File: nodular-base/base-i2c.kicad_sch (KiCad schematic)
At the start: 4 parts, among them U4 TCA9548APWR, U7 SC7A20

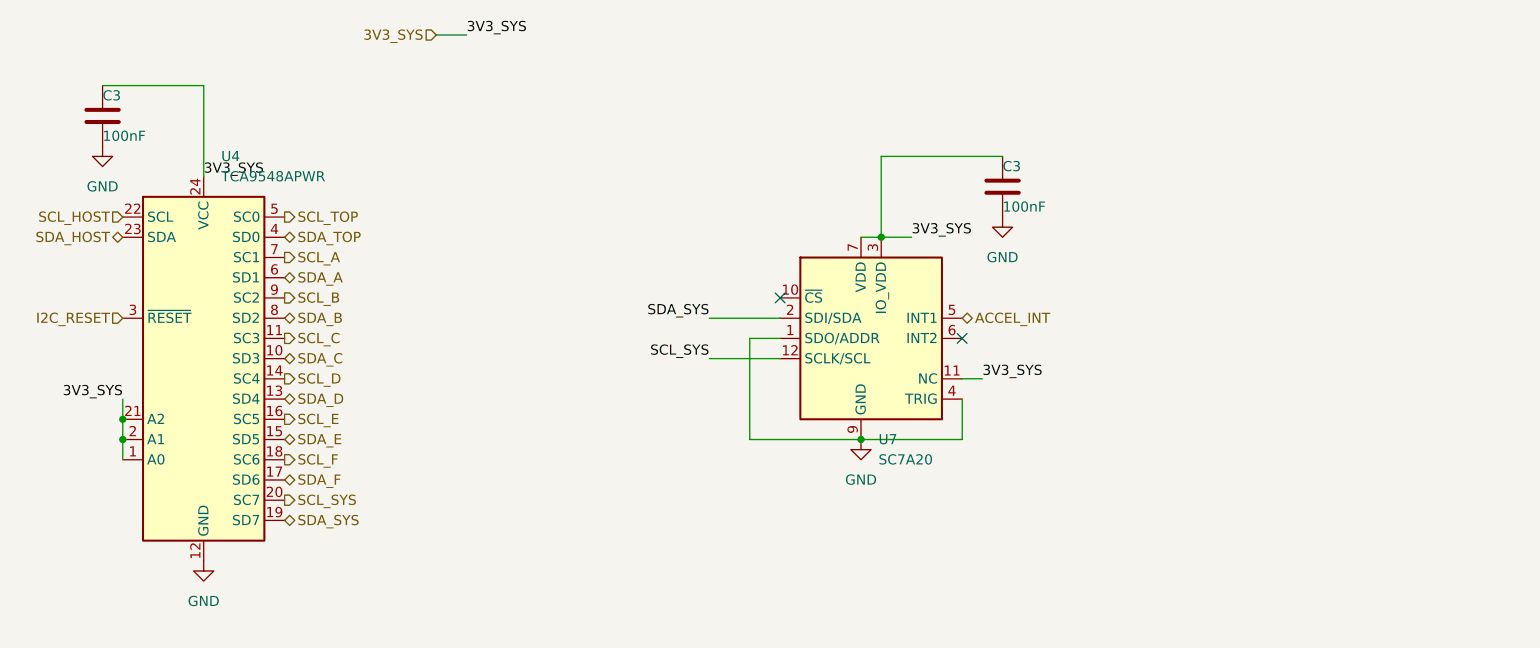
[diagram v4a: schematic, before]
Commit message: Add additional accelerometer-gyro option, update pin and address map, fix some ERC errors
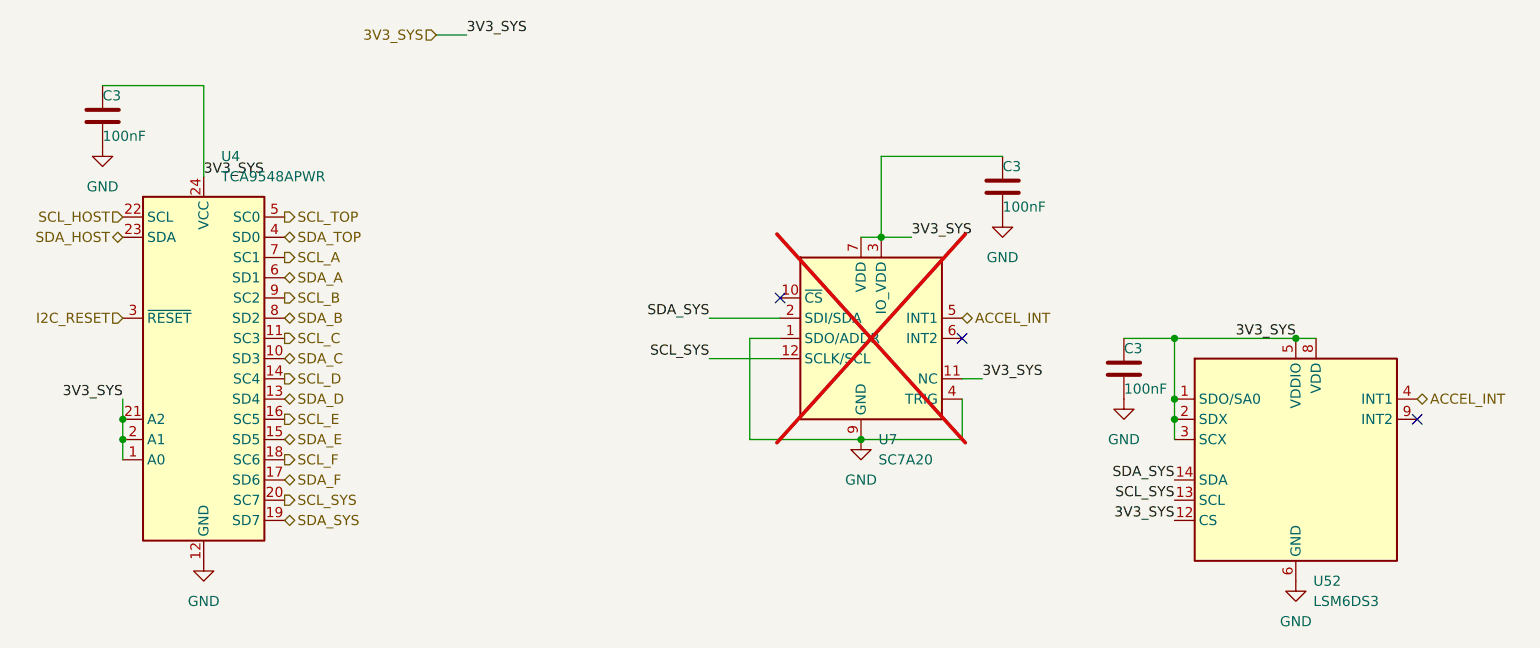
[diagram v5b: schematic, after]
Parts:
- added C3: 100nF, Capacitor_SMD:C_0402_1005Metric, symbol Device:C
- added U52: LSM6DS3, Package_LGA:LGA-14_3x2.5mm_P0.5mm_LayoutBorder3x4y, symbol Sensor_Motion:LSM6DS3
- U7: now not fitted
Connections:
- net 3V3_SYS: now also C3.1, U52.1 (SDO/SA0), U52.12 (CS), U52.2 (SDX), U52.3 (SCX), U52.5 (VDDIO), U52.8 (VDD)
- net ACCEL_INT: now also U52.4 (INT1)
- net GND: now also C3.2, U52.6 (GND), U52.7 (GND)
- net SCL_SYS: now also U52.13 (SCL)
- net SDA_SYS: now also U52.14 (SDA)
- no-connect marks 2 -> 3
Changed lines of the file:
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@@
 (kicad_sch (version 20230121) (generator eeschema)
   (paper "A4")
+  (junction (at 234.95 80.01) (diameter 0) (color 0 0 0 0)
+  )
+  (junction (at 234.95 82.55) (diameter 0) (color 0 0 0 0)
+  )
   (junction (at 102.87 85.09) (diameter 0) (color 0 0 0 0)
   )
+  (junction (at 250.19 72.39) (diameter 0) (color 0 0 0 0)
+  )
   (junction (at 102.87 82.55) (diameter 0) (color 0 0 0 0)
+  )
+  (junction (at 234.95 72.39) (diameter 0) (color 0 0 0 0)
   )
   (junction (at 198.12 59.69) (diameter 0) (color 0 0 0 0)
@@
   (no_connect (at 208.28 72.39))
   (no_connect (at 185.42 67.31))
+  (no_connect (at 265.43 82.55))
   (wire (pts (xy 102.87 82.55) (xy 102.87 85.09))
     (stroke (width 0) (type default))
@@
     (stroke (width 0) (type default))
   )
+  (wire (pts (xy 234.95 80.01) (xy 234.95 72.39))
+    (stroke (width 0) (type default))
+  )
   (wire (pts (xy 213.36 49.53) (xy 198.12 49.53))
     (stroke (width 0) (type default))
   )
+  (wire (pts (xy 228.6 72.39) (xy 234.95 72.39))
+    (stroke (width 0) (type default))
+  )
   (wire (pts (xy 102.87 80.01) (xy 102.87 82.55))
     (stroke (width 0) (type default))
@@
     (stroke (width 0) (type default))
   )
+  (wire (pts (xy 234.95 82.55) (xy 234.95 80.01))
+    (stroke (width 0) (type default))
+  )
   (wire (pts (xy 113.03 52.07) (xy 113.03 40.64))
     (stroke (width 0) (type default))
   )
+  (wire (pts (xy 234.95 85.09) (xy 234.95 82.55))
+    (stroke (width 0) (type default))
+  )
   (wire (pts (xy 195.58 59.69) (xy 198.12 59.69))
     (stroke (width 0) (type default))
   )
+  (wire (pts (xy 234.95 72.39) (xy 250.19 72.39))
+    (stroke (width 0) (type default))
+  )
   (wire (pts (xy 198.12 49.53) (xy 198.12 59.69))
     (stroke (width 0) (type default))
@@
   )
   (wire (pts (xy 208.28 80.01) (xy 208.28 85.09))
+    (stroke (width 0) (type default))
+  )
+  (wire (pts (xy 250.19 72.39) (xy 252.73 72.39))
     (stroke (width 0) (type default))
   )
@@
     (effects (font (size 1.27 1.27)) (justify left bottom))
   )
+  (label "3V3_SYS" (at 234.95 95.25 180) (fields_autoplaced)
+    (effects (font (size 1.27 1.27)) (justify right bottom))
+  )
+  (label "SCL_SYS" (at 234.95 92.71 180) (fields_autoplaced)
+    (effects (font (size 1.27 1.27)) (justify right bottom))
+  )
   (label "SCL_SYS" (at 176.53 74.93 180) (fields_autoplaced)
+    (effects (font (size 1.27 1.27)) (justify right bottom))
+  )
+  (label "3V3_SYS" (at 250.19 72.39 180) (fields_autoplaced)
+    (effects (font (size 1.27 1.27)) (justify right bottom))
+  )
+  (label "SDA_SYS" (at 234.95 90.17 180) (fields_autoplaced)
     (effects (font (size 1.27 1.27)) (justify right bottom))
   )
@@
     (effects (font (size 1.27 1.27)) (justify left))
   )
+  (hierarchical_label "ACCEL_INT" (shape bidirectional) (at 265.43 80.01 0) (fields_autoplaced)
+    (effects (font (size 1.27 1.27)) (justify left))
+  )
   (hierarchical_label "SCL_A" (shape output) (at 123.19 62.23 0) (fields_autoplaced)
     (effects (font (size 1.27 1.27)) (justify left))
+  )
+  (symbol (lib_id "power:GND") (at 250.19 102.87 0) (unit 1)
+    (in_bom yes) (on_board yes) (dnp no) (fields_autoplaced)
+    (property "Reference" "#PWR070" (at 250.19 109.22 0)
+      (effects (font (size 1.27 1.27)) hide)
+    )
+    (property "Value" "GND" (at 250.19 107.95 0)
+      (effects (font (size 1.27 1.27)))
+    )
+    (property "Footprint" "" (at 250.19 102.87 0)
+      (effects (font (size 1.27 1.27)) hide)
+    )
+    (property "Datasheet" "" (at 250.19 102.87 0)
+      (effects (font (size 1.27 1.27)) hide)
+    )
+    (pin "1")
+    (instances
+      (project "nodular-base"
+        (path "/6dcb0502-87e2-4c28-9ce8-81aab8925f06/5ae693f9-48f3-406c-bbdf-b76d81cc71eb"
+          (reference "#PWR070") (unit 1)
+        )
+      )
+    )
   )
   (symbol (lib_id "Interface_Expansion:TCA9548APWR") (at 113.03 74.93 0) (unit 1)
@@
     )
   )
+  (symbol (lib_id "power:GND") (at 228.6 80.01 0) (unit 1)
+    (in_bom yes) (on_board yes) (dnp no) (fields_autoplaced)
+    (property "Reference" "#PWR071" (at 228.6 86.36 0)
+      (effects (font (size 1.27 1.27)) hide)
+    )
+    (property "Value" "GND" (at 228.6 85.09 0)
+      (effects (font (size 1.27 1.27)))
+    )
+    (property "Footprint" "" (at 228.6 80.01 0)
+      (effects (font (size 1.27 1.27)) hide)
+    )
+    (property "Datasheet" "" (at 228.6 80.01 0)
+      (effects (font (size 1.27 1.27)) hide)
+    )
+    (pin "1")
+    (instances
+      (project "nodular-base"
+        (path "/6dcb0502-87e2-4c28-9ce8-81aab8925f06/5ae693f9-48f3-406c-bbdf-b76d81cc71eb"
+          (reference "#PWR071") (unit 1)
+        )
+      )
+    )
+  )
   (symbol (lib_id "Device:C") (at 100.33 44.45 0) (unit 1)
     (in_bom yes) (on_board yes) (dnp no)
@@
     )
   )
+  (symbol (lib_id "Device:C") (at 228.6 76.2 0) (unit 1)
+    (in_bom yes) (on_board yes) (dnp no)
+    (property "Reference" "C3" (at 228.6 73.66 0)
+      (effects (font (size 1.27 1.27)) (justify left))
+    )
+    (property "Value" "100nF" (at 228.6 78.74 0)
+      (effects (font (size 1.27 1.27)) (justify left))
+    )
+    (property "Footprint" "Capacitor_SMD:C_0402_1005Metric" (at 229.5652 80.01 0)
+      (effects (font (size 1.27 1.27)) hide)
+    )
+    (property "Datasheet" "~" (at 228.6 76.2 0)
+      (effects (font (size 1.27 1.27)) hide)
+    )
+    (pin "1")
+    (pin "2")
+    (instances
+      (project "nodular-base"
+        (path "/6dcb0502-87e2-4c28-9ce8-81aab8925f06"
+          (reference "C3") (unit 1)
+        )
+        (path "/6dcb0502-87e2-4c28-9ce8-81aab8925f06/5ae693f9-48f3-406c-bbdf-b76d81cc71eb"
+          (reference "C50") (unit 1)
+        )
+      )
+    )
+  )
   (symbol (lib_id "power:GND") (at 213.36 57.15 0) (unit 1)
     (in_bom yes) (on_board yes) (dnp no) (fields_autoplaced)
@@
     )
   )
+  (symbol (lib_id "Sensor_Motion:LSM6DS3") (at 250.19 87.63 0) (unit 1)
+    (in_bom yes) (on_board yes) (dnp no) (fields_autoplaced)
+    (property "Reference" "U52" (at 252.3841 102.87 0)
+      (effects (font (size 1.27 1.27)) (justify left))
+    )
+    (property "Value" "LSM6DS3" (at 252.3841 105.41 0)
+      (effects (font (size 1.27 1.27)) (justify left))
+    )
+    (property "Footprint" "Package_LGA:LGA-14_3x2.5mm_P0.5mm_LayoutBorder3x4y" (at 240.03 105.41 0)
+      (effects (font (size 1.27 1.27)) (justify left) hide)
+    )
+    (property "Datasheet" "https://www.st.com/resource/en/datasheet/lsm6ds3tr-c.pdf" (at 252.73 104.14 0)
+      (effects (font (size 1.27 1.27)) hide)
+    )
+    (pin "13")
+    (pin "11")
+    (pin "2")
+    (pin "12")
+    (pin "7")
+    (pin "14")
+    (pin "5")
+    (pin "6")
+    (pin "8")
+    (pin "4")
+    (pin "3")
+    (pin "10")
+    (pin "9")
+    (pin "1")
+    (instances
+      (project "nodular-base"
+        (path "/6dcb0502-87e2-4c28-9ce8-81aab8925f06/5ae693f9-48f3-406c-bbdf-b76d81cc71eb"
+          (reference "U52") (unit 1)
+        )
+      )
+    )
+  )
   (symbol (lib_id "power:GND") (at 100.33 48.26 0) (unit 1)
     (in_bom yes) (on_board yes) (dnp no) (fields_autoplaced)
@@
   )
   (symbol (lib_id "Sensor_Motion:KX022-1020") (at 195.58 72.39 0) (unit 1)
-    (in_bom yes) (on_board yes) (dnp no) (fields_autoplaced)
+    (in_bom yes) (on_board yes) (dnp yes) (fields_autoplaced)
     (property "Reference" "U7" (at 197.7741 85.09 0)
       (effects (font (size 1.27 1.27)) (justify left))

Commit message: Modify base board: - Fix ESP32 strapping pins state - Remove 3/6 M3 standoffs - Change to LGA-style pads on ESP32 - Modify SFP mechanical pads to not be plated - Add larger mechanical pads with more solder paste surface to USB-C connectors
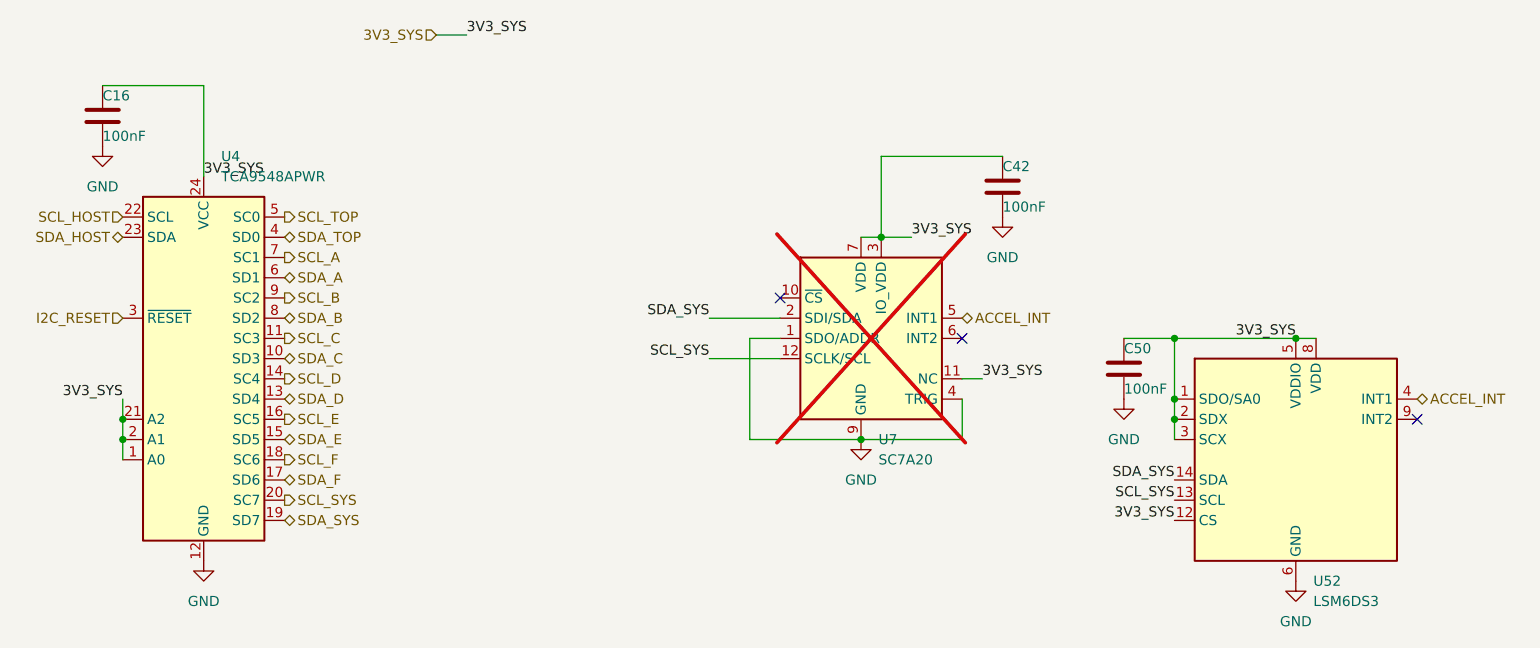
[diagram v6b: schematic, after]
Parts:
- renumbered C3 to C16, C3 to C42, C3 to C50
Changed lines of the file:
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@@
   (symbol (lib_id "Device:C") (at 213.36 53.34 0) (unit 1)
     (in_bom yes) (on_board yes) (dnp no)
-    (property "Reference" "C3" (at 213.36 50.8 0)
+    (property "Reference" "C42" (at 213.36 50.8 0)
       (effects (font (size 1.27 1.27)) (justify left))
     )
@@
     (instances
       (project "nodular-base"
-        (path "/6dcb0502-87e2-4c28-9ce8-81aab8925f06"
-          (reference "C3") (unit 1)
-        )
         (path "/6dcb0502-87e2-4c28-9ce8-81aab8925f06/5ae693f9-48f3-406c-bbdf-b76d81cc71eb"
           (reference "C42") (unit 1)
@@
   (symbol (lib_id "Device:C") (at 100.33 44.45 0) (unit 1)
     (in_bom yes) (on_board yes) (dnp no)
-    (property "Reference" "C3" (at 100.33 41.91 0)
+    (property "Reference" "C16" (at 100.33 41.91 0)
       (effects (font (size 1.27 1.27)) (justify left))
     )
@@
     (instances
       (project "nodular-base"
-        (path "/6dcb0502-87e2-4c28-9ce8-81aab8925f06"
-          (reference "C3") (unit 1)
-        )
         (path "/6dcb0502-87e2-4c28-9ce8-81aab8925f06/5ae693f9-48f3-406c-bbdf-b76d81cc71eb"
           (reference "C16") (unit 1)
@@
   (symbol (lib_id "Device:C") (at 228.6 76.2 0) (unit 1)
     (in_bom yes) (on_board yes) (dnp no)
-    (property "Reference" "C3" (at 228.6 73.66 0)
+    (property "Reference" "C50" (at 228.6 73.66 0)
       (effects (font (size 1.27 1.27)) (justify left))
     )
@@
     (instances
       (project "nodular-base"
-        (path "/6dcb0502-87e2-4c28-9ce8-81aab8925f06"
-          (reference "C3") (unit 1)
-        )
         (path "/6dcb0502-87e2-4c28-9ce8-81aab8925f06/5ae693f9-48f3-406c-bbdf-b76d81cc71eb"
           (reference "C50") (unit 1)
